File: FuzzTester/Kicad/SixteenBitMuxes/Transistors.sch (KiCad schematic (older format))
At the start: 20 parts, among them Q1 PN2222A, Q10 2SC1815, Q12 S9013, Q14 S9018, Q15 BC848B, Q16 2SC1623, Q17 MPSA18, Q19 2N5088, Q2 MMBT3904, Q3 MMBT5551L, Q4 MMBTA42, Q5 BC807, Q6 BC846, Q7 BC847B, Q8 BC847C, Q9 C945, U8 CD4067BM, U9 CD4067BM

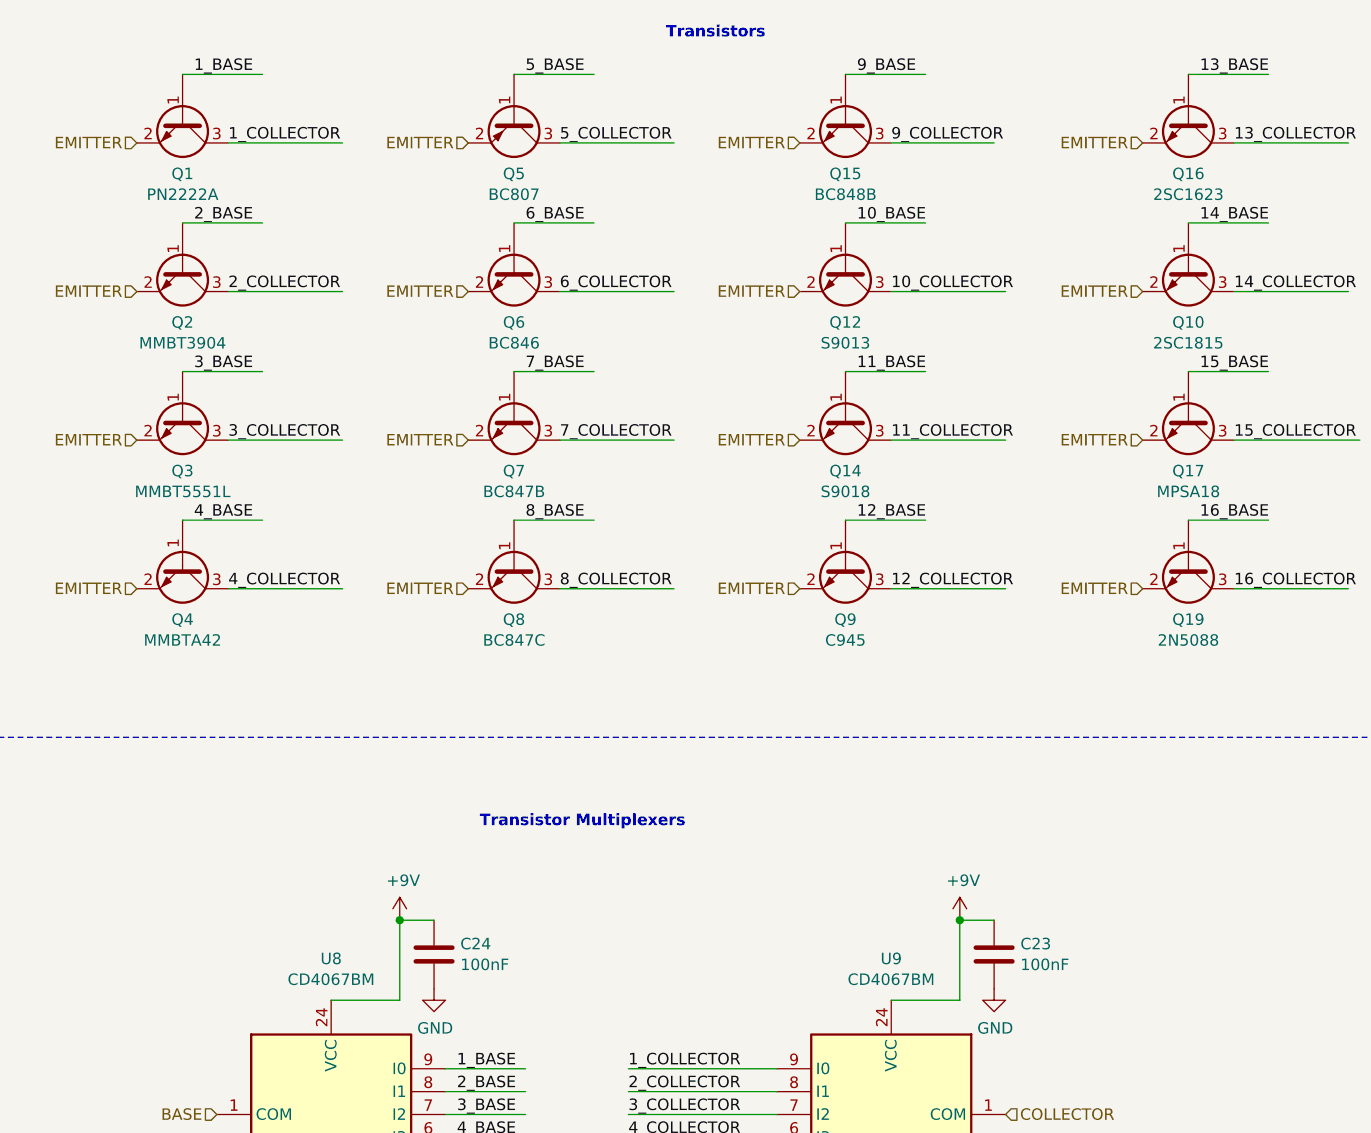
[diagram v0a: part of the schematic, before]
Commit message: Removed shift registers
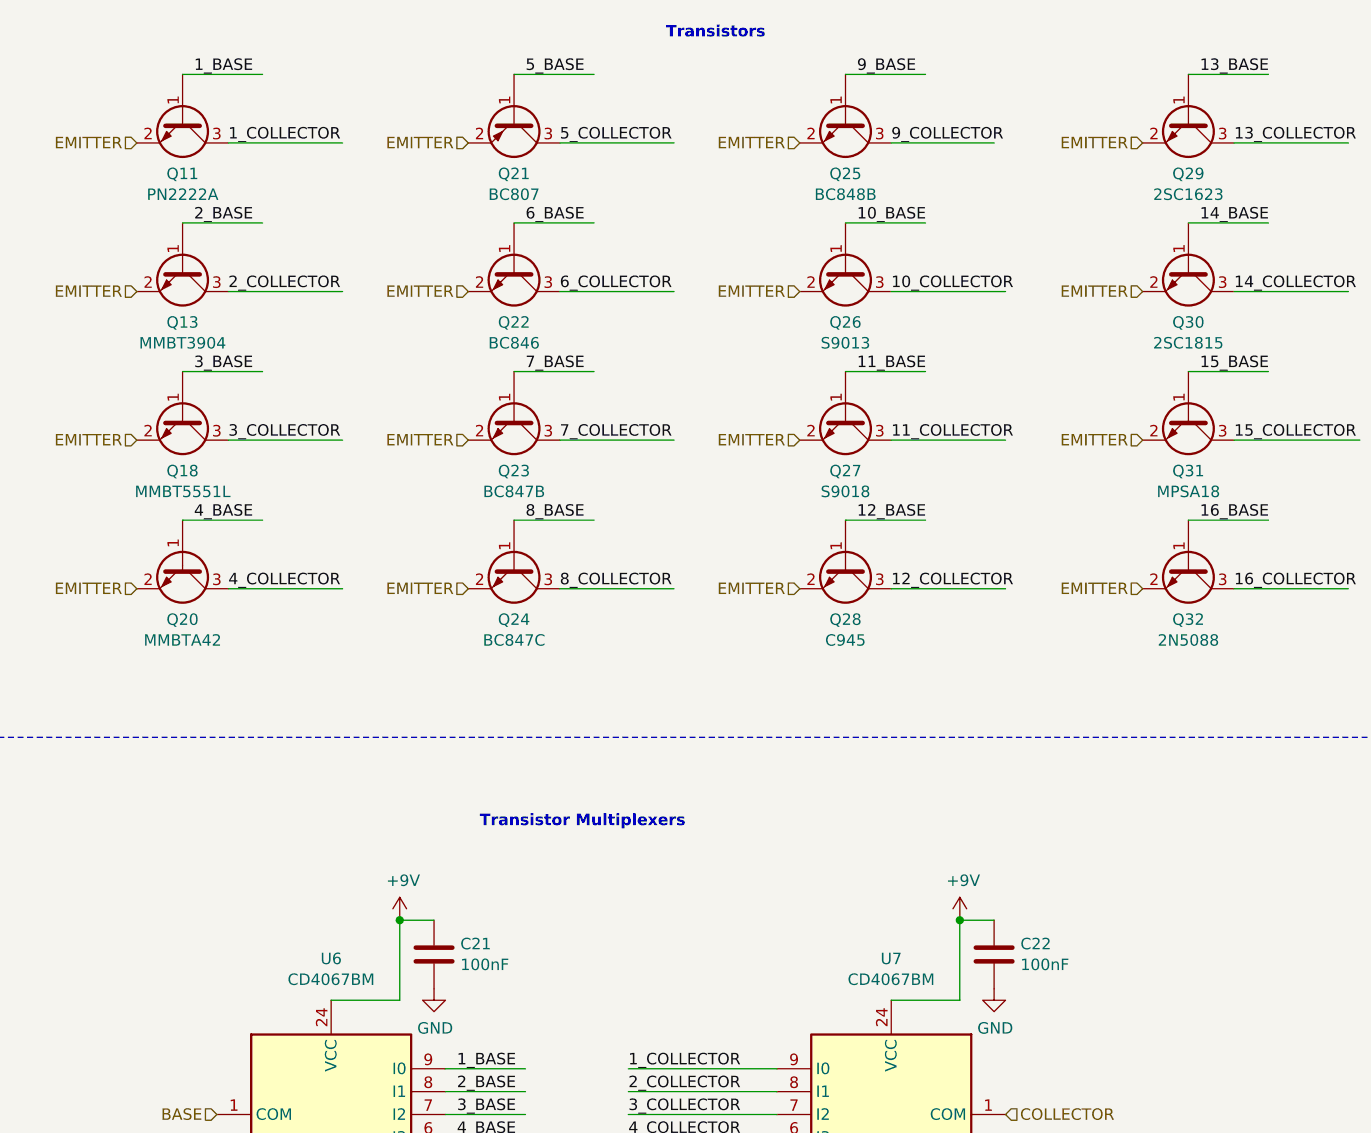
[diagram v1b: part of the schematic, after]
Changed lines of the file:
@@
 $Descr A4 11693 8268
 encoding utf-8
-Sheet 7 11
+Sheet 8 9
 Title "Guitar Pedal Effect Fuzz Digitally Controlled"
 Date "2020-04-07"
@@
 AR Path="/5F9746B8/5EA993A8" Ref="Q24"  Part="1"
 AR Path="/5ED1AB26/5EA993A8" Ref="Q20"  Part="1"
-F 0 "Q4" V 1835 3400 50  0000 C CNN
+F 0 "Q20" V 1835 3400 50  0000 C CNN
 F 1 "MMBTA42" V 1926 3400 50  0000 C CNN
 F 2 "Package_TO_SOT_SMD:SOT-23_Handsoldering" H 1800 3325 50  0001 L CIN
@@
 AR Path="/5F9746B8/5EA993B4" Ref="Q39"  Part="1"
 AR Path="/5ED1AB26/5EA993B4" Ref="Q32"  Part="1"
-F 0 "Q19" V 6235 3400 50  0000 C CNN
+F 0 "Q32" V 6235 3400 50  0000 C CNN
 F 1 "2N5088" V 6326 3400 50  0000 C CNN
 F 2 "Package_TO_SOT_THT:TO-92_Inline" H 6200 3325 50  0001 L CIN
@@
 AR Path="/5F9746B8/5EA993C0" Ref="Q37"  Part="1"
 AR Path="/5ED1AB26/5EA993C0" Ref="Q31"  Part="1"
-F 0 "Q17" V 6235 2750 50  0000 C CNN
+F 0 "Q31" V 6235 2750 50  0000 C CNN
 F 1 "MPSA18" V 6326 2750 50  0000 C CNN
 F 2 "Package_TO_SOT_THT:TO-92_Inline" H 6200 2675 50  0001 L CIN
@@
 AR Path="/5F9746B8/5EA993CD" Ref="Q36"  Part="1"
 AR Path="/5ED1AB26/5EA993CD" Ref="Q29"  Part="1"
-F 0 "Q16" V 6235 1450 50  0000 C CNN
+F 0 "Q29" V 6235 1450 50  0000 C CNN
 F 1 "2SC1623" V 6326 1450 50  0000 C CNN
 F 2 "Package_TO_SOT_SMD:SOT-23_Handsoldering" H 6200 1550 50  0001 C CNN
@@
 AR Path="/5F9746B8/5EA993FC" Ref="Q28"  Part="1"
 AR Path="/5ED1AB26/5EA993FC" Ref="Q24"  Part="1"
-F 0 "Q8" V 3285 3400 50  0000 C CNN
+F 0 "Q24" V 3285 3400 50  0000 C CNN
 F 1 "BC847C" V 3376 3400 50  0000 C CNN
 F 2 "Package_TO_SOT_SMD:SOT-23_Handsoldering" H 3250 3325 50  0001 L CIN
@@
 AR Path="/5F9746B8/5EA99402" Ref="Q27"  Part="1"
 AR Path="/5ED1AB26/5EA99402" Ref="Q23"  Part="1"
-F 0 "Q7" V 3285 2750 50  0000 C CNN
+F 0 "Q23" V 3285 2750 50  0000 C CNN
 F 1 "BC847B" V 3376 2750 50  0000 C CNN
 F 2 "Package_TO_SOT_SMD:SOT-23_Handsoldering" H 3250 2850 50  0001 C CNN
@@
 AR Path="/5F9746B8/5EA99408" Ref="Q26"  Part="1"
 AR Path="/5ED1AB26/5EA99408" Ref="Q22"  Part="1"
-F 0 "Q6" V 3285 2100 50  0000 C CNN
+F 0 "Q22" V 3285 2100 50  0000 C CNN
 F 1 "BC846" V 3376 2100 50  0000 C CNN
 F 2 "Package_TO_SOT_SMD:SOT-23_Handsoldering" H 3250 2025 50  0001 L CIN
@@
 AR Path="/5F9746B8/5EA9940E" Ref="Q25"  Part="1"
 AR Path="/5ED1AB26/5EA9940E" Ref="Q21"  Part="1"
-F 0 "Q5" V 3285 1450 50  0000 C CNN
+F 0 "Q21" V 3285 1450 50  0000 C CNN
 F 1 "BC807" V 3376 1450 50  0000 C CNN
 F 2 "Package_TO_SOT_SMD:SOT-23_Handsoldering" H 3250 1375 50  0001 L CIN
@@
 AR Path="/5F9746B8/5EA99637" Ref="Q23"  Part="1"
 AR Path="/5ED1AB26/5EA99637" Ref="Q18"  Part="1"
-F 0 "Q3" V 1835 2750 50  0000 C CNN
+F 0 "Q18" V 1835 2750 50  0000 C CNN
 F 1 "MMBT5551L" V 1926 2750 50  0000 C CNN
 F 2 "Package_TO_SOT_SMD:SOT-23_Handsoldering" H 1800 2675 50  0001 L CIN
@@
 AR Path="/5F9746B8/5EA99643" Ref="Q22"  Part="1"
 AR Path="/5ED1AB26/5EA99643" Ref="Q13"  Part="1"
-F 0 "Q2" V 1835 2100 50  0000 C CNN
+F 0 "Q13" V 1835 2100 50  0000 C CNN
 F 1 "MMBT3904" V 1926 2100 50  0000 C CNN
 F 2 "Package_TO_SOT_SMD:SOT-23_Handsoldering" H 1800 2025 50  0001 L CIN
@@
 AR Path="/5F9746B8/5F014460" Ref="Q30"  Part="1"
 AR Path="/5ED1AB26/5F014460" Ref="Q30"  Part="1"
-F 0 "Q10" V 6235 2100 50  0000 C CNN
+F 0 "Q30" V 6235 2100 50  0000 C CNN
 F 1 "2SC1815" V 6326 2100 50  0000 C CNN
 F 2 "Package_TO_SOT_SMD:SOT-23_Handsoldering" H 6200 2025 50  0001 L CIN
@@
 AR Path="/5F9746B8/5F02F005" Ref="Q29"  Part="1"
 AR Path="/5ED1AB26/5F02F005" Ref="Q28"  Part="1"
-F 0 "Q9" V 4735 3400 50  0000 C CNN
+F 0 "Q28" V 4735 3400 50  0000 C CNN
 F 1 "C945" V 4826 3400 50  0000 C CNN
 F 2 "Package_TO_SOT_SMD:SOT-23_Handsoldering" H 4700 3500 50  0001 C CNN
@@
 AR Path="/5F9746B8/5EA9963D" Ref="Q21"  Part="1"
 AR Path="/5ED1AB26/5EA9963D" Ref="Q11"  Part="1"
-F 0 "Q1" V 1835 1450 50  0000 C CNN
+F 0 "Q11" V 1835 1450 50  0000 C CNN
 F 1 "PN2222A" V 1926 1450 50  0000 C CNN
 F 2 "Package_TO_SOT_SMD:SOT-23_Handsoldering" H 1800 1375 50  0001 L CIN
@@
 AR Path="/5F9746B8/5EA993C7" Ref="Q35"  Part="1"
 AR Path="/5ED1AB26/5EA993C7" Ref="Q25"  Part="1"
-F 0 "Q15" V 4735 1450 50  0000 C CNN
+F 0 "Q25" V 4735 1450 50  0000 C CNN
 F 1 "BC848B" V 4826 1450 50  0000 C CNN
 F 2 "Package_TO_SOT_SMD:SOT-23_Handsoldering" H 4700 1375 50  0001 L CIN
@@
 AR Path="/5F9746B8/5EA993D3" Ref="Q34"  Part="1"
 AR Path="/5ED1AB26/5EA993D3" Ref="Q27"  Part="1"
-F 0 "Q14" V 4735 2750 50  0000 C CNN
+F 0 "Q27" V 4735 2750 50  0000 C CNN
 F 1 "S9018" V 4826 2750 50  0000 C CNN
 F 2 "Package_TO_SOT_SMD:SOT-23_Handsoldering" H 4700 2850 50  0001 C CNN
@@
 AR Path="/5F9746B8/5EA993DF" Ref="Q32"  Part="1"
 AR Path="/5ED1AB26/5EA993DF" Ref="Q26"  Part="1"
-F 0 "Q12" V 4735 2100 50  0000 C CNN
+F 0 "Q26" V 4735 2100 50  0000 C CNN
 F 1 "S9013" V 4826 2100 50  0000 C CNN
 F 2 "Package_TO_SOT_SMD:SOT-23_Handsoldering" H 4700 2200 50  0001 C CNN
@@
 AR Path="/5E9AE796/5EA4E538" Ref="U9"  Part="1"
 AR Path="/5ED1AB26/5EA4E538" Ref="U7"  Part="1"
-F 0 "U9" H 4700 7481 50  0000 C CNN
+F 0 "U7" H 4700 7481 50  0000 C CNN
 F 1 "CD4067BM" H 4700 7390 50  0000 C CNN
 F 2 "Package_SO:SOIC-24W_7.5x15.4mm_P1.27mm" H 5600 5300 50  0001 C CIN
@@
 AR Path="/5E9AE796/5EA3E429" Ref="U8"  Part="1"
 AR Path="/5ED1AB26/5EA3E429" Ref="U6"  Part="1"
-F 0 "U8" H 2250 7481 50  0000 C CNN
+F 0 "U6" H 2250 7481 50  0000 C CNN
 F 1 "CD4067BM" H 2250 7390 50  0000 C CNN
 F 2 "Package_SO:SOIC-24W_7.5x15.4mm_P1.27mm" H 3150 5300 50  0001 C CIN
@@
 AR Path="/5F9746B8/5EA99533" Ref="C31"  Part="1"
 AR Path="/5ED1AB26/5EA99533" Ref="C21"  Part="1"
-F 0 "C24" H 2815 5146 50  0000 L CNN
+F 0 "C21" H 2815 5146 50  0000 L CNN
 F 1 "100nF" H 2815 5055 50  0000 L CNN
 F 2 "Capacitor_SMD:C_0805_2012Metric_Pad1.15x1.40mm_HandSolder" H 2738 4950 50  0001 C CNN
@@
 AR Path="/5F9746B8/5ECDF6D6" Ref="C?"  Part="1"
 AR Path="/5ED1AB26/5ECDF6D6" Ref="C22"  Part="1"
-F 0 "C23" H 5265 5146 50  0000 L CNN
+F 0 "C22" H 5265 5146 50  0000 L CNN
 F 1 "100nF" H 5265 5055 50  0000 L CNN
 F 2 "Capacitor_SMD:C_0805_2012Metric_Pad1.15x1.40mm_HandSolder" H 5188 4950 50  0001 C CNN

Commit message: Finished (but not beautiful) PCB without SPI and most 8 channel multiplexers.
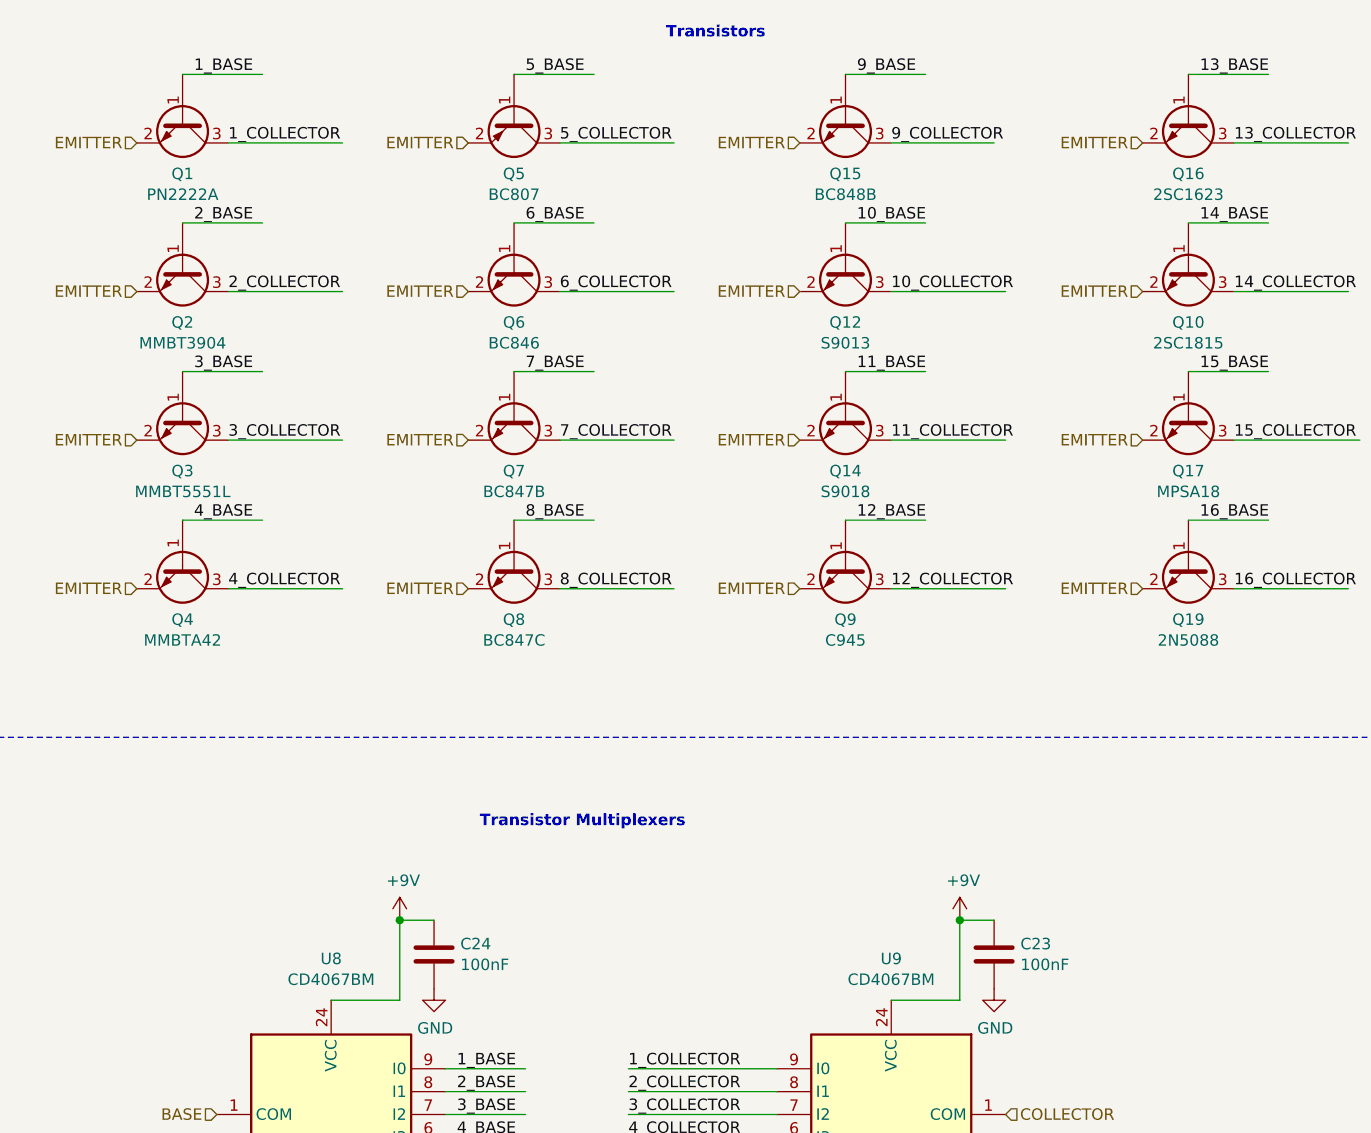
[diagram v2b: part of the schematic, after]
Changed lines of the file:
@@
 AR Path="/5F9746B8/5EA993A8" Ref="Q24"  Part="1"
 AR Path="/5ED1AB26/5EA993A8" Ref="Q20"  Part="1"
-F 0 "Q20" V 1835 3400 50  0000 C CNN
+F 0 "Q4" V 1835 3400 50  0000 C CNN
 F 1 "MMBTA42" V 1926 3400 50  0000 C CNN
 F 2 "Package_TO_SOT_SMD:SOT-23_Handsoldering" H 1800 3325 50  0001 L CIN
@@
 AR Path="/5F9746B8/5EA993B4" Ref="Q39"  Part="1"
 AR Path="/5ED1AB26/5EA993B4" Ref="Q32"  Part="1"
-F 0 "Q32" V 6235 3400 50  0000 C CNN
+F 0 "Q19" V 6235 3400 50  0000 C CNN
 F 1 "2N5088" V 6326 3400 50  0000 C CNN
 F 2 "Package_TO_SOT_THT:TO-92_Inline" H 6200 3325 50  0001 L CIN
@@
 AR Path="/5F9746B8/5EA993C0" Ref="Q37"  Part="1"
 AR Path="/5ED1AB26/5EA993C0" Ref="Q31"  Part="1"
-F 0 "Q31" V 6235 2750 50  0000 C CNN
+F 0 "Q17" V 6235 2750 50  0000 C CNN
 F 1 "MPSA18" V 6326 2750 50  0000 C CNN
 F 2 "Package_TO_SOT_THT:TO-92_Inline" H 6200 2675 50  0001 L CIN
@@
 AR Path="/5F9746B8/5EA993CD" Ref="Q36"  Part="1"
 AR Path="/5ED1AB26/5EA993CD" Ref="Q29"  Part="1"
-F 0 "Q29" V 6235 1450 50  0000 C CNN
+F 0 "Q16" V 6235 1450 50  0000 C CNN
 F 1 "2SC1623" V 6326 1450 50  0000 C CNN
 F 2 "Package_TO_SOT_SMD:SOT-23_Handsoldering" H 6200 1550 50  0001 C CNN
@@
 AR Path="/5F9746B8/5EA993FC" Ref="Q28"  Part="1"
 AR Path="/5ED1AB26/5EA993FC" Ref="Q24"  Part="1"
-F 0 "Q24" V 3285 3400 50  0000 C CNN
+F 0 "Q8" V 3285 3400 50  0000 C CNN
 F 1 "BC847C" V 3376 3400 50  0000 C CNN
 F 2 "Package_TO_SOT_SMD:SOT-23_Handsoldering" H 3250 3325 50  0001 L CIN
@@
 AR Path="/5F9746B8/5EA99402" Ref="Q27"  Part="1"
 AR Path="/5ED1AB26/5EA99402" Ref="Q23"  Part="1"
-F 0 "Q23" V 3285 2750 50  0000 C CNN
+F 0 "Q7" V 3285 2750 50  0000 C CNN
 F 1 "BC847B" V 3376 2750 50  0000 C CNN
 F 2 "Package_TO_SOT_SMD:SOT-23_Handsoldering" H 3250 2850 50  0001 C CNN
@@
 AR Path="/5F9746B8/5EA99408" Ref="Q26"  Part="1"
 AR Path="/5ED1AB26/5EA99408" Ref="Q22"  Part="1"
-F 0 "Q22" V 3285 2100 50  0000 C CNN
+F 0 "Q6" V 3285 2100 50  0000 C CNN
 F 1 "BC846" V 3376 2100 50  0000 C CNN
 F 2 "Package_TO_SOT_SMD:SOT-23_Handsoldering" H 3250 2025 50  0001 L CIN
@@
 AR Path="/5F9746B8/5EA9940E" Ref="Q25"  Part="1"
 AR Path="/5ED1AB26/5EA9940E" Ref="Q21"  Part="1"
-F 0 "Q21" V 3285 1450 50  0000 C CNN
+F 0 "Q5" V 3285 1450 50  0000 C CNN
 F 1 "BC807" V 3376 1450 50  0000 C CNN
 F 2 "Package_TO_SOT_SMD:SOT-23_Handsoldering" H 3250 1375 50  0001 L CIN
@@
 AR Path="/5F9746B8/5EA99637" Ref="Q23"  Part="1"
 AR Path="/5ED1AB26/5EA99637" Ref="Q18"  Part="1"
-F 0 "Q18" V 1835 2750 50  0000 C CNN
+F 0 "Q3" V 1835 2750 50  0000 C CNN
 F 1 "MMBT5551L" V 1926 2750 50  0000 C CNN
 F 2 "Package_TO_SOT_SMD:SOT-23_Handsoldering" H 1800 2675 50  0001 L CIN
@@
 AR Path="/5F9746B8/5EA99643" Ref="Q22"  Part="1"
 AR Path="/5ED1AB26/5EA99643" Ref="Q13"  Part="1"
-F 0 "Q13" V 1835 2100 50  0000 C CNN
+F 0 "Q2" V 1835 2100 50  0000 C CNN
 F 1 "MMBT3904" V 1926 2100 50  0000 C CNN
 F 2 "Package_TO_SOT_SMD:SOT-23_Handsoldering" H 1800 2025 50  0001 L CIN
@@
 AR Path="/5F9746B8/5F014460" Ref="Q30"  Part="1"
 AR Path="/5ED1AB26/5F014460" Ref="Q30"  Part="1"
-F 0 "Q30" V 6235 2100 50  0000 C CNN
+F 0 "Q10" V 6235 2100 50  0000 C CNN
 F 1 "2SC1815" V 6326 2100 50  0000 C CNN
 F 2 "Package_TO_SOT_SMD:SOT-23_Handsoldering" H 6200 2025 50  0001 L CIN
@@
 AR Path="/5F9746B8/5F02F005" Ref="Q29"  Part="1"
 AR Path="/5ED1AB26/5F02F005" Ref="Q28"  Part="1"
-F 0 "Q28" V 4735 3400 50  0000 C CNN
+F 0 "Q9" V 4735 3400 50  0000 C CNN
 F 1 "C945" V 4826 3400 50  0000 C CNN
 F 2 "Package_TO_SOT_SMD:SOT-23_Handsoldering" H 4700 3500 50  0001 C CNN
@@
 AR Path="/5F9746B8/5EA9963D" Ref="Q21"  Part="1"
 AR Path="/5ED1AB26/5EA9963D" Ref="Q11"  Part="1"
-F 0 "Q11" V 1835 1450 50  0000 C CNN
+F 0 "Q1" V 1835 1450 50  0000 C CNN
 F 1 "PN2222A" V 1926 1450 50  0000 C CNN
 F 2 "Package_TO_SOT_SMD:SOT-23_Handsoldering" H 1800 1375 50  0001 L CIN
@@
 AR Path="/5F9746B8/5EA993C7" Ref="Q35"  Part="1"
 AR Path="/5ED1AB26/5EA993C7" Ref="Q25"  Part="1"
-F 0 "Q25" V 4735 1450 50  0000 C CNN
+F 0 "Q15" V 4735 1450 50  0000 C CNN
 F 1 "BC848B" V 4826 1450 50  0000 C CNN
 F 2 "Package_TO_SOT_SMD:SOT-23_Handsoldering" H 4700 1375 50  0001 L CIN
@@
 AR Path="/5F9746B8/5EA993D3" Ref="Q34"  Part="1"
 AR Path="/5ED1AB26/5EA993D3" Ref="Q27"  Part="1"
-F 0 "Q27" V 4735 2750 50  0000 C CNN
+F 0 "Q14" V 4735 2750 50  0000 C CNN
 F 1 "S9018" V 4826 2750 50  0000 C CNN
 F 2 "Package_TO_SOT_SMD:SOT-23_Handsoldering" H 4700 2850 50  0001 C CNN
@@
 AR Path="/5F9746B8/5EA993DF" Ref="Q32"  Part="1"
 AR Path="/5ED1AB26/5EA993DF" Ref="Q26"  Part="1"
-F 0 "Q26" V 4735 2100 50  0000 C CNN
+F 0 "Q12" V 4735 2100 50  0000 C CNN
 F 1 "S9013" V 4826 2100 50  0000 C CNN
 F 2 "Package_TO_SOT_SMD:SOT-23_Handsoldering" H 4700 2200 50  0001 C CNN
@@
 AR Path="/5E9AE796/5EA4E538" Ref="U9"  Part="1"
 AR Path="/5ED1AB26/5EA4E538" Ref="U7"  Part="1"
-F 0 "U7" H 4700 7481 50  0000 C CNN
+F 0 "U9" H 4700 7481 50  0000 C CNN
 F 1 "CD4067BM" H 4700 7390 50  0000 C CNN
 F 2 "Package_SO:SOIC-24W_7.5x15.4mm_P1.27mm" H 5600 5300 50  0001 C CIN
@@
 AR Path="/5E9AE796/5EA3E429" Ref="U8"  Part="1"
 AR Path="/5ED1AB26/5EA3E429" Ref="U6"  Part="1"
-F 0 "U6" H 2250 7481 50  0000 C CNN
+F 0 "U8" H 2250 7481 50  0000 C CNN
 F 1 "CD4067BM" H 2250 7390 50  0000 C CNN
 F 2 "Package_SO:SOIC-24W_7.5x15.4mm_P1.27mm" H 3150 5300 50  0001 C CIN
@@
 AR Path="/5F9746B8/5EA99533" Ref="C31"  Part="1"
 AR Path="/5ED1AB26/5EA99533" Ref="C21"  Part="1"
-F 0 "C21" H 2815 5146 50  0000 L CNN
+F 0 "C24" H 2815 5146 50  0000 L CNN
 F 1 "100nF" H 2815 5055 50  0000 L CNN
 F 2 "Capacitor_SMD:C_0805_2012Metric_Pad1.15x1.40mm_HandSolder" H 2738 4950 50  0001 C CNN
@@
 AR Path="/5F9746B8/5ECDF6D6" Ref="C?"  Part="1"
 AR Path="/5ED1AB26/5ECDF6D6" Ref="C22"  Part="1"
-F 0 "C22" H 5265 5146 50  0000 L CNN
+F 0 "C23" H 5265 5146 50  0000 L CNN
 F 1 "100nF" H 5265 5055 50  0000 L CNN
 F 2 "Capacitor_SMD:C_0805_2012Metric_Pad1.15x1.40mm_HandSolder" H 5188 4950 50  0001 C CNN
